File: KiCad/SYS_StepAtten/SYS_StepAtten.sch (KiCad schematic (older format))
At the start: 119 parts, among them J1 RCA-1, J2 RCA-2, J3 AUX-1-2, J4 Barrel_Jack 9Vac, J5 POT_EXT Conn, J6 cfg jumper, J7 ARM SWD, J8 RCA-Out, K1 G6K-2F-Y, K10 G6K-2F-Y, K11 G6K-2F-Y, K12 G6K-2F-Y, K13 G6K-2F-Y, K14 G6K-2F-Y, K2 G6K-2F-Y, K3 G6K-2F-Y, K4 G6K-2F-Y, K5 G6K-2F-Y, K6 G6K-2F-Y, K7 G6K-2F-Y, K8 G6K-2F-Y, K9 G6K-2F-Y, Q1 2N7002, Q10 2N7002, Q11 2N7002, Q12 2N7002, Q13 2N7002, Q14 2N7002, Q2 2N7002, Q3 2N7002, Q4 2N7002, Q5 2N7002, Q6 2N7002, Q7 2N7002, Q8 2N7002, Q9 2N7002, SW1 ON/OFF, SW2 INPUT_SWITCH, U1 LM317, U2 STM32f030K6T6, Y1 8Mhz

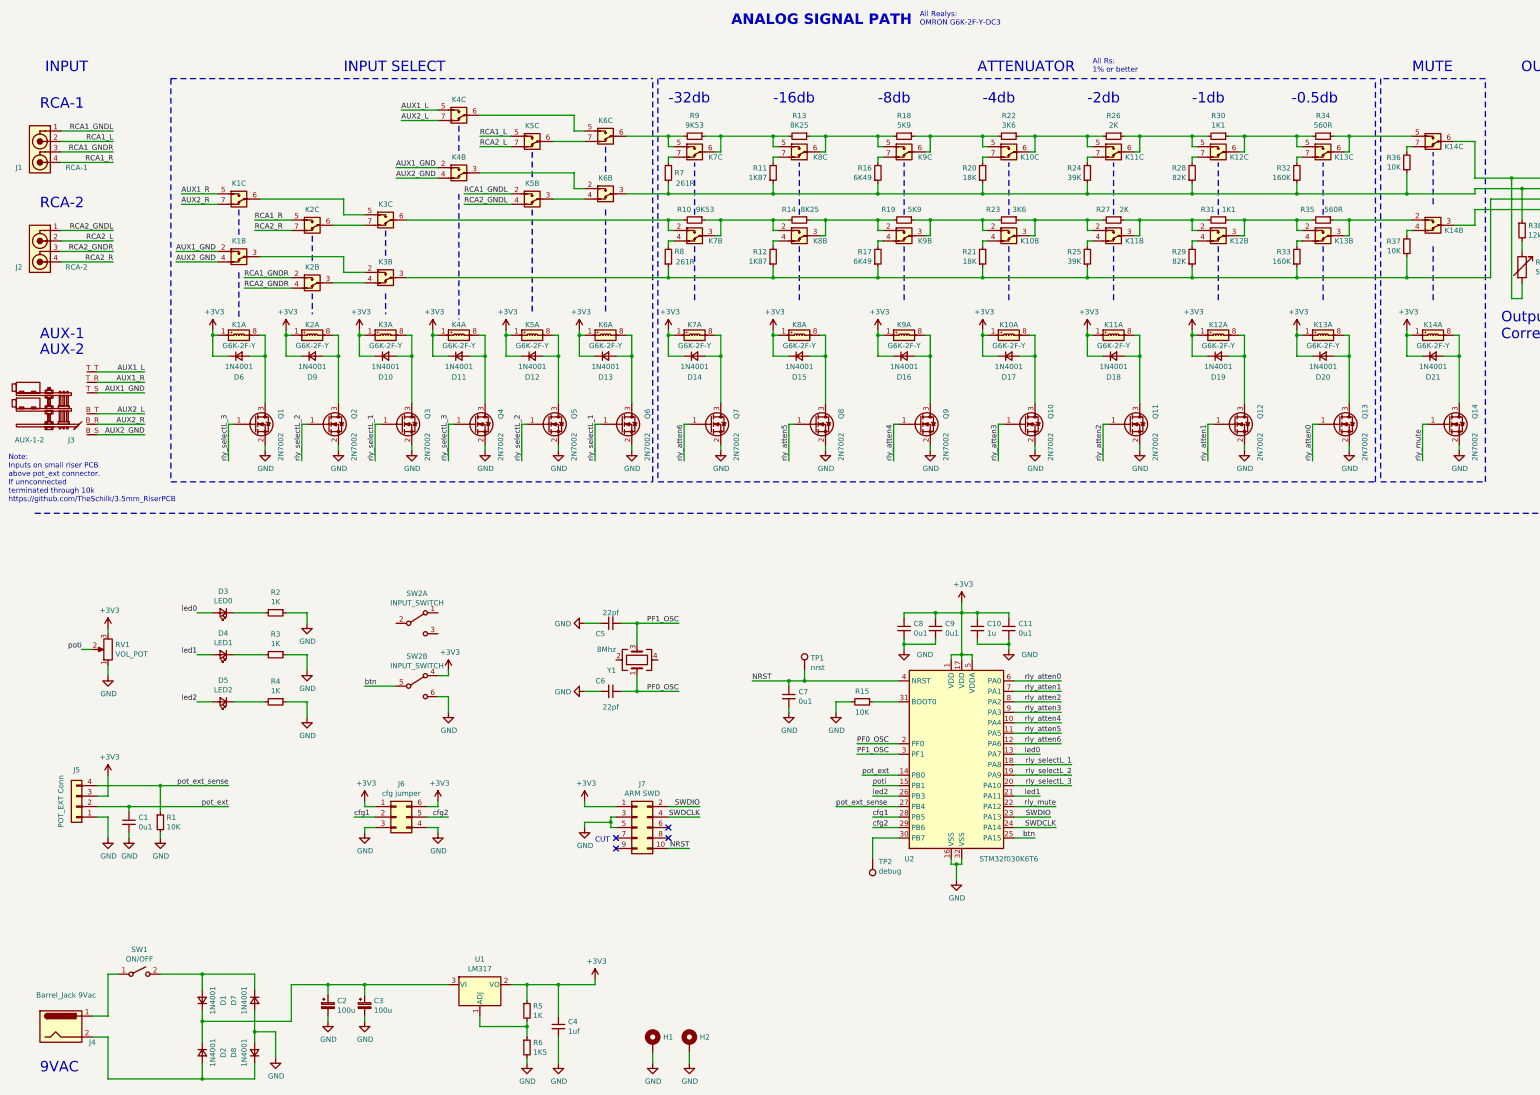
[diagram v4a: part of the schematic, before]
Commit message: Schematic Refinments, Changed Relays and moved to own power rail
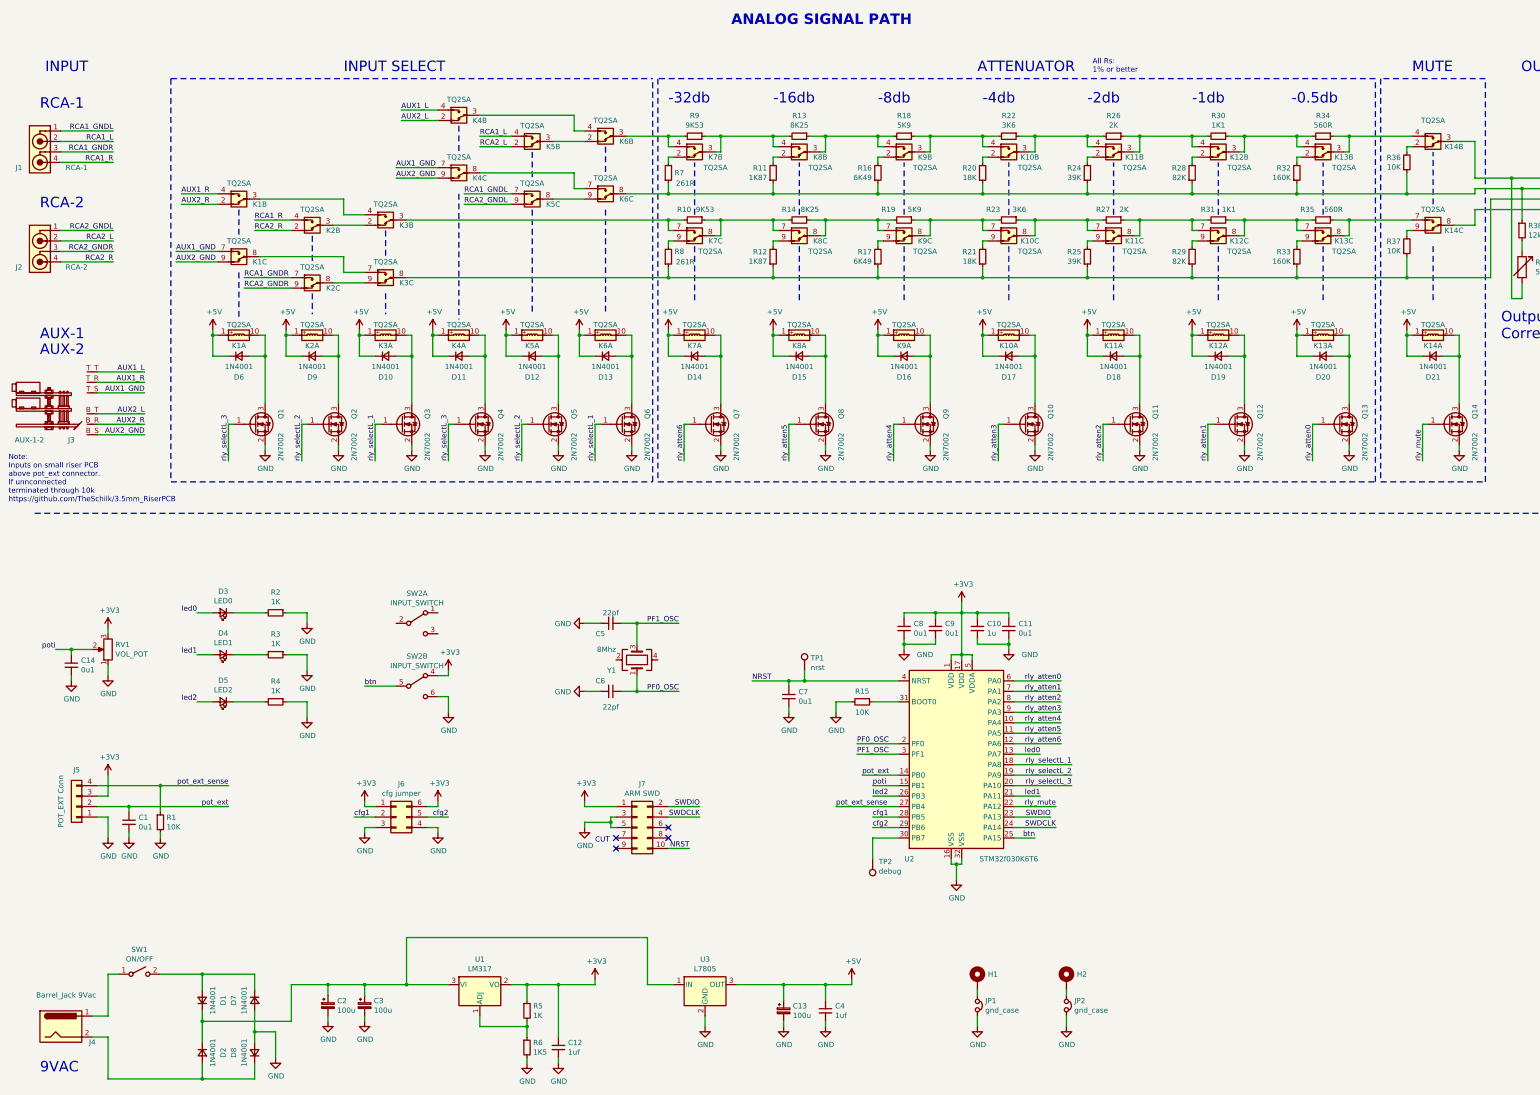
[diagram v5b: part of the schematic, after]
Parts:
- removed K1, K10, K11, K12, K13, K14, K2, K3, K4, K5, K6, K7, K8, K9: G6K-2F-Y, OMRON_G6K-2F-Y:OMRON_G6K-2F-Y, symbol OMRON_G6K-2F-Y:G6K-2F-Y-Multi
- added C12: 1uf, Capacitor_SMD:C_0603_1608Metric, symbol Device:C_Small
- added C13: 100u, Capacitor_SMD:CP_Elec_8x6.9, symbol Device:CP_Small
- added C14: 0u1, Capacitor_SMD:C_0603_1608Metric, symbol Device:C_Small
- added JP1, JP2: gnd_case, Resistor_SMD:R_0603_1608Metric, symbol Device:Jumper_NC_Small
- added K1, K10, K11, K12, K13, K14, K2, K3, K4, K5, K6, K7, K8, K9: TQ2SA, Panasonic_TQ2SA:Panasonic_TQ2SA, symbol Panasonic_TQ2SA:TQ2SA-Multi
- added U3: L7805, Package_TO_SOT_SMD:TO-252-2, symbol Regulator_Linear:L7805
- J5: footprint Connector_PinHeader_2.54mm:PinHeader_1x04_P2.54mm_Horizontal -> Connector_PinHeader_2.54mm:PinHeader_2x02_P2.54mm_Horizontal
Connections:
- net +3V3: now also C12.1; no longer C4.1, D10.1 (K), D11.1 (K), D12.1 (K), D13.1 (K), D14.1 (K), D15.1 (K), D16.1 (K), D17.1 (K), D18.1 (K), D19.1 (K), D20.1 (K), D21.1 (K), D6.1 (K), D9.1 (K)
- net AUX1_GND: now also K1.7, K4.7
- net AUX1_L: now also K4.4
- net AUX1_R: now also K1.4
- net AUX2_GND: now also K1.9, K4.9
- net AUX2_L: now also K4.2
- net AUX2_R: now also K1.2
- net GND: now also C12.2, C13.2, C14.2, JP1.2, JP2.2, U3.2 (GND); no longer H1.1, H2.1
- net RCA1_GNDL: now also K5.7
- net RCA1_GNDR: now also K2.7
- net RCA1_L: now also K5.4
- net RCA1_R: now also K2.4
- net RCA2_GNDL: now also K5.9
- net RCA2_GNDR: now also K2.9
- net RCA2_L: now also K5.2
- net RCA2_R: now also K2.2
- net poti: now also C14.1
- net at D14.2 (A), Q7.3 (D): now also K7.10
- net at R10.2: now also K3.3, K7.7
- net at R10.1, R14.2: now also K7.8, K8.7
- net at R8.2: now also K7.9
- net at R9.2: now also K6.3, K7.4
- net at R13.2, R9.1: now also K7.3, K8.4
- net at R7.2: now also K7.2
- net at J8.2, R11.1, R16.1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: now also K6.8
- net at J8.3, R12.1, R17.1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: now also K3.8
- net at D15.2 (A), Q8.3 (D): now also K8.10
- net at R14.1, R19.2: now also K8.8, K9.7
- net at R12.2: now also K8.9
- net at R13.1, R18.2: now also K8.3, K9.4
- net at R11.2: now also K8.2
- net at D16.2 (A), Q9.3 (D): now also K9.10
- net at R19.1, R23.2: now also K10.7, K9.8
- net at R17.2: now also K9.9
- net at R18.1, R22.2: now also K10.4, K9.3
- net at R16.2: now also K9.2
- net at D17.2 (A), Q10.3 (D): now also K10.10
- net at R23.1, R27.2: now also K10.8, K11.7
- net at R21.2: now also K10.9
- net at R22.1, R26.2: now also K10.3, K11.4
- net at R20.2: now also K10.2
- net at D18.2 (A), Q11.3 (D): now also K11.10
- net at R27.1, R31.2: now also K11.8, K12.7
- net at R25.2: now also K11.9
- net at R26.1, R30.2: now also K11.3, K12.4
- net at R24.2: now also K11.2
- net at D19.2 (A), Q12.3 (D): now also K12.10
- net at R31.1, R35.2: now also K12.8, K13.7
- net at R29.2: now also K12.9
- net at R30.1, R34.2: now also K12.3, K13.4
- net at R28.2: now also K12.2
- net at D20.2 (A), Q13.3 (D): now also K13.10
- net at R35.1: now also K13.8, K14.7
- net at R33.2: now also K13.9
- net at R34.1: now also K13.3, K14.4
- net at R32.2: now also K13.2
- net at J8.1, R39.2: now also K14.3
- net at R36.2: now also K14.2
- net at J8.4, R40.1: now also K14.8
- net at R37.2: now also K14.9
- net at D21.2 (A), Q14.3 (D): now also K14.10
- net at D13.2 (A), Q6.3 (D): now also K6.10
- net at D11.2 (A), Q4.3 (D): now also K4.10
- net at D9.2 (A), Q2.3 (D): now also K2.10
- net at D10.2 (A), Q3.3 (D): now also K3.10
- net at D12.2 (A), Q5.3 (D): now also K5.10
- net at C2.1, C3.1, D1.1 (K)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: now also U3.1 (IN)
- net at D6.2 (A), Q1.3 (D): now also K1.10
- new net: H1.1, JP1.1
- new net: K1.8, K3.7
- new net: K1.3, K3.4
- new net: H2.1, JP2.1
- new net: K2.3, K3.2
- new net: K2.8, K3.9
- new net: K4.3, K6.4
- new net: K4.8, K6.7
- new net: K5.3, K6.2
- new net: K5.8, K6.9
- new net +5V: C13.1, C4.1, D10.1 (K), D11.1 (K), D12.1 (K), D13.1 (K), D14.1 (K), D15.1 (K), D16.1 (K), D17.1 (K), D18.1 (K), D19.1 (K), D20.1 (K), D21.1 (K), D6.1 (K), D9.1 (K), K1.1, K10.1, K11.1, K12.1, K13.1, K14.1, K2.1, K3.1, K4.1, K5.1, K6.1, K7.1, K8.1, K9.1, U3.3 (OUT)
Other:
- note removed: "All Realys:\nOMRON G6K-2F-Y-DC3\n"
- moved on the sheet: C4, H1, H2

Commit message: Basic Sorting Done
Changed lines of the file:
@@
 P 3650 10300
 F 0 "#PWR0109" H 3650 10050 50  0001 C CNN
-F 1 "GND" H 3655 10127 50  0000 C CNN
+F 1 "GND" H 3650 10150 50  0000 C CNN
 F 2 "" H 3650 10300 50  0001 C CNN
 F 3 "" H 3650 10300 50  0001 C CNN

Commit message: finished testing board v0.0
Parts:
- removed J6: cfg jumper, Connector_PinHeader_2.54mm:PinHeader_2x03_P2.54mm_Vertical, symbol Connector_Generic:Conn_02x03_Counter_Clockwise
- added J6: cfg jumper, Connector_PinHeader_2.54mm:PinHeader_2x03_P2.54mm_Vertical, symbol Connector_Generic:Conn_02x03_Odd_Even
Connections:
- net +3V3: now also J6.1 (Pin_1), J6.2 (Pin_2)
- net GND: now also J6.5 (Pin_5), J6.6 (Pin_6)
- net cfg1: now also J6.3 (Pin_3)
- net cfg2: now also J6.4 (Pin_4)
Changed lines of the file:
@@
-$EndComp
-$Comp
-L Connector_Generic:Conn_02x03_Counter_Clockwise J6
-U 1 1 66013D22
-P 4300 8350
-F 0 "J6" H 4350 8667 50  0000 C CNN
-F 1 "cfg jumper" H 4350 8576 50  0000 C CNN
-F 2 "Connector_PinHeader_2.54mm:PinHeader_2x03_P2.54mm_Vertical" H 4300 8350 50  0001 C CNN
-F 3 "~" H 4300 8350 50  0001 C CNN
-	1    4300 8350
-	1    0    0    -1
 $EndComp
 $Comp
@@
 Wire Wire Line
 	1200 6750 1400 6750
+$Comp
+L Connector_Generic:Conn_02x03_Odd_Even J6
+U 1 1 5ED7C887
+P 4300 8350
+F 0 "J6" H 4350 8667 50  0000 C CNN
+F 1 "cfg jumper" H 4350 8576 50  0000 C CNN
+F 2 "Connector_PinHeader_2.54mm:PinHeader_2x03_P2.54mm_Vertical" H 4300 8350 50  0001 C CNN
+F 3 "~" H 4300 8350 50  0001 C CNN
+	1    4300 8350
+	1    0    0    -1
+$EndComp
 $EndSCHEMATC
